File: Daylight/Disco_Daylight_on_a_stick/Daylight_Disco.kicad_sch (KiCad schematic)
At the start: 38 parts, among them J1 Conn_01x03_Male, J2 Conn_01x03_Male, J3 Conn_01x01_Male

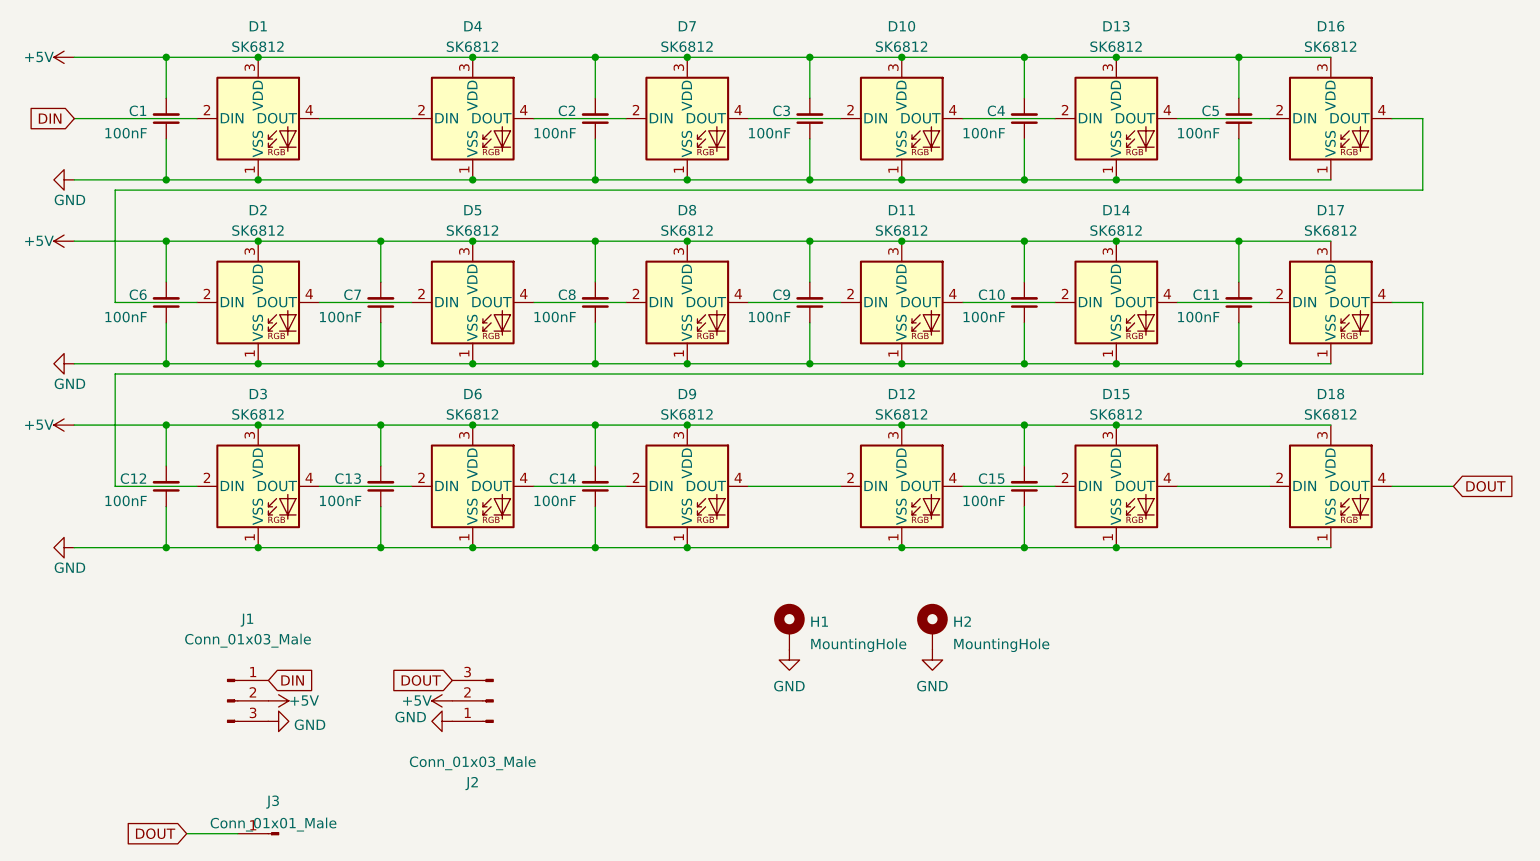
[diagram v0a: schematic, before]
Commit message: Finished first version of the Daylight & Disco Sticks. Turned all leds by 90°. Rerouted tracks to be more efficient. Ordered first verison of this from jlcpcb.
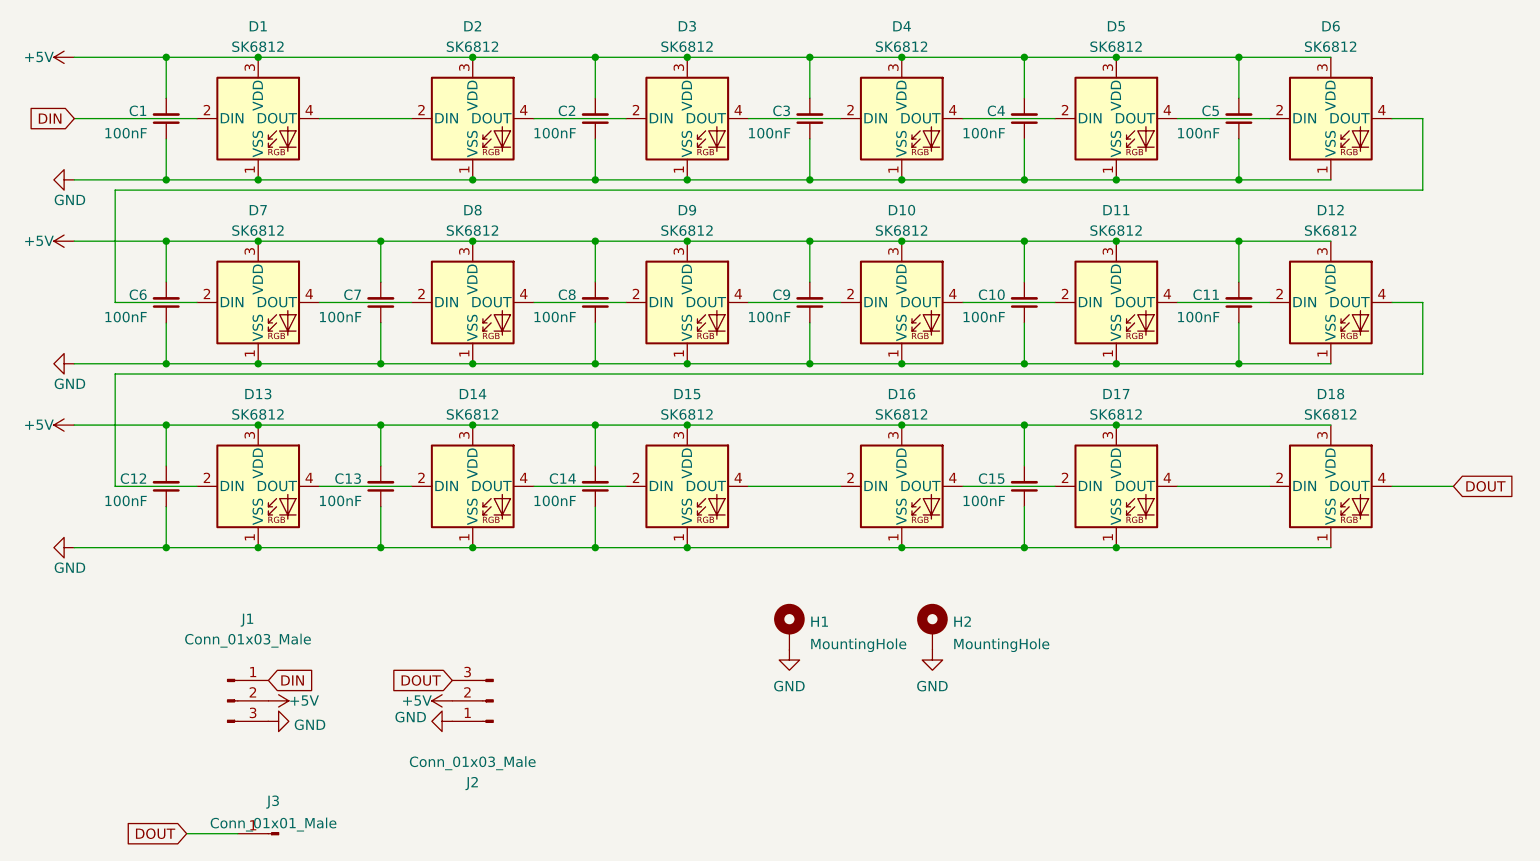
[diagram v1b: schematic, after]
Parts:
- renumbered D11 to D10, D14 to D11, D17 to D12, D3 to D13, D6 to D14, D9 to D15, D12 to D16, D15 to D17, D4 to D2, D7 to D3, D10 to D4, D13 to D5, D16 to D6, D2 to D7, D5 to D8, D8 to D9
